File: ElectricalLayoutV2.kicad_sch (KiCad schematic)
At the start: 8 parts, among them J1 PowerBar (24V), J2 PowerBar (Ground), K1 5V-24V (40A), SW1 BFB, SW2 Dead man's switch

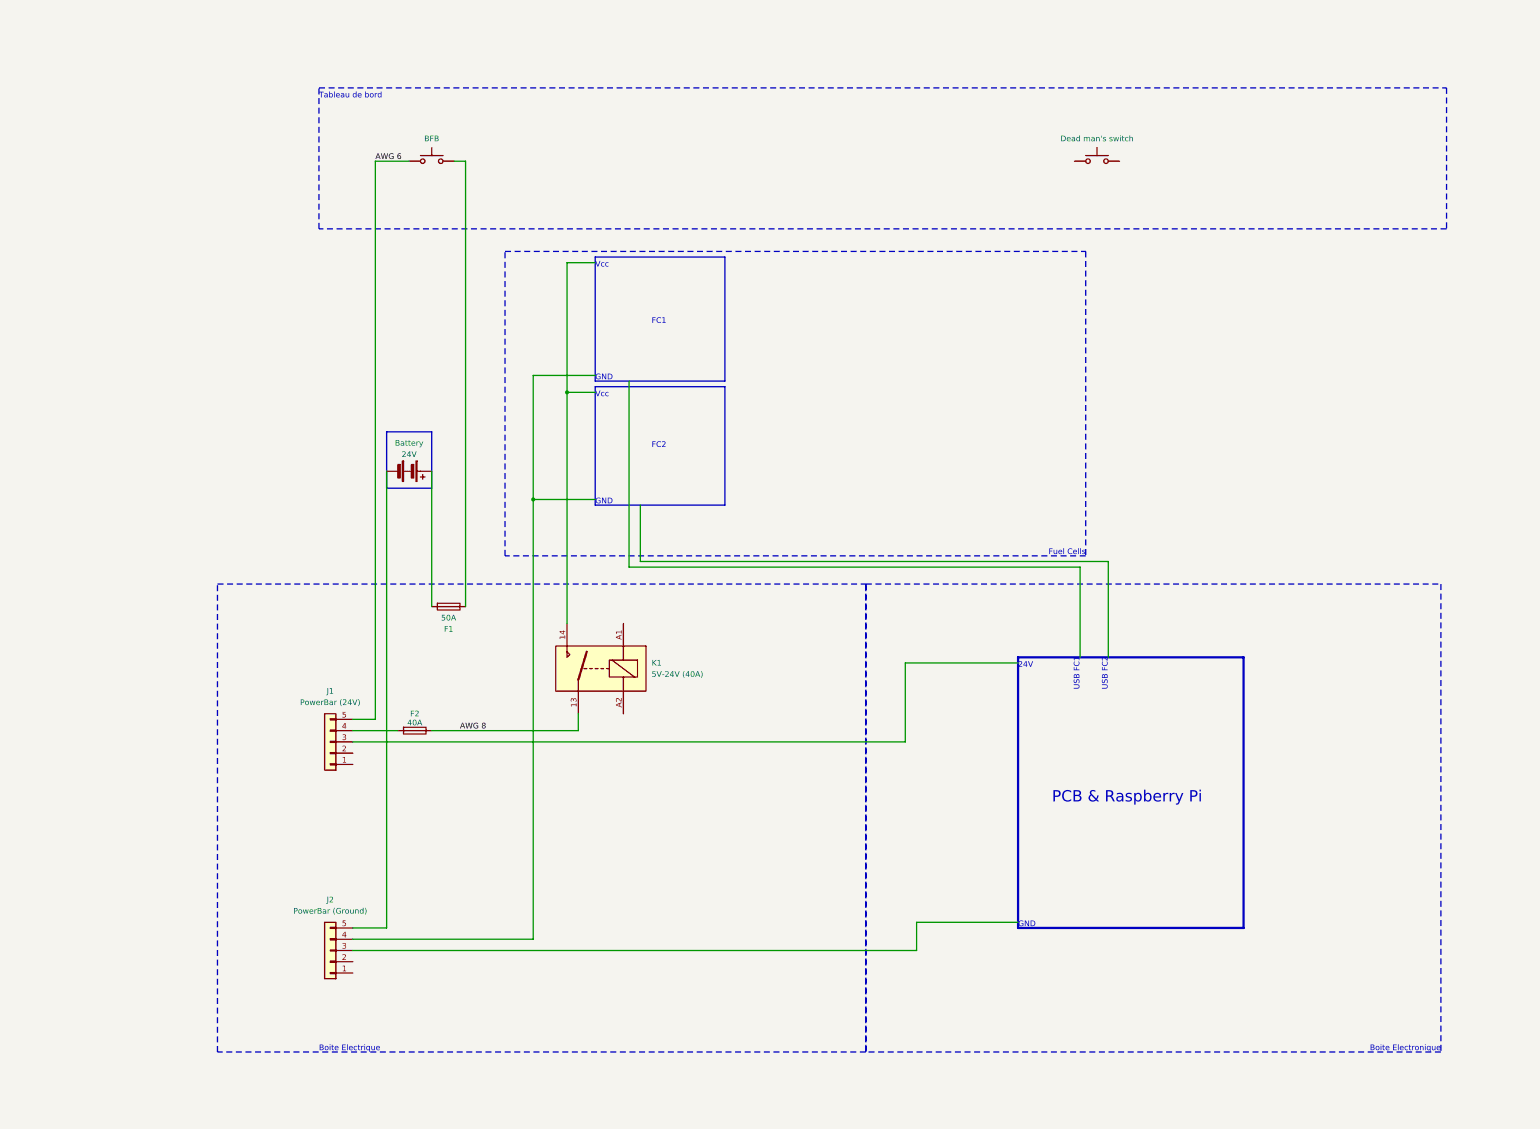
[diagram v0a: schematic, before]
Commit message: Fuel cells and precharge
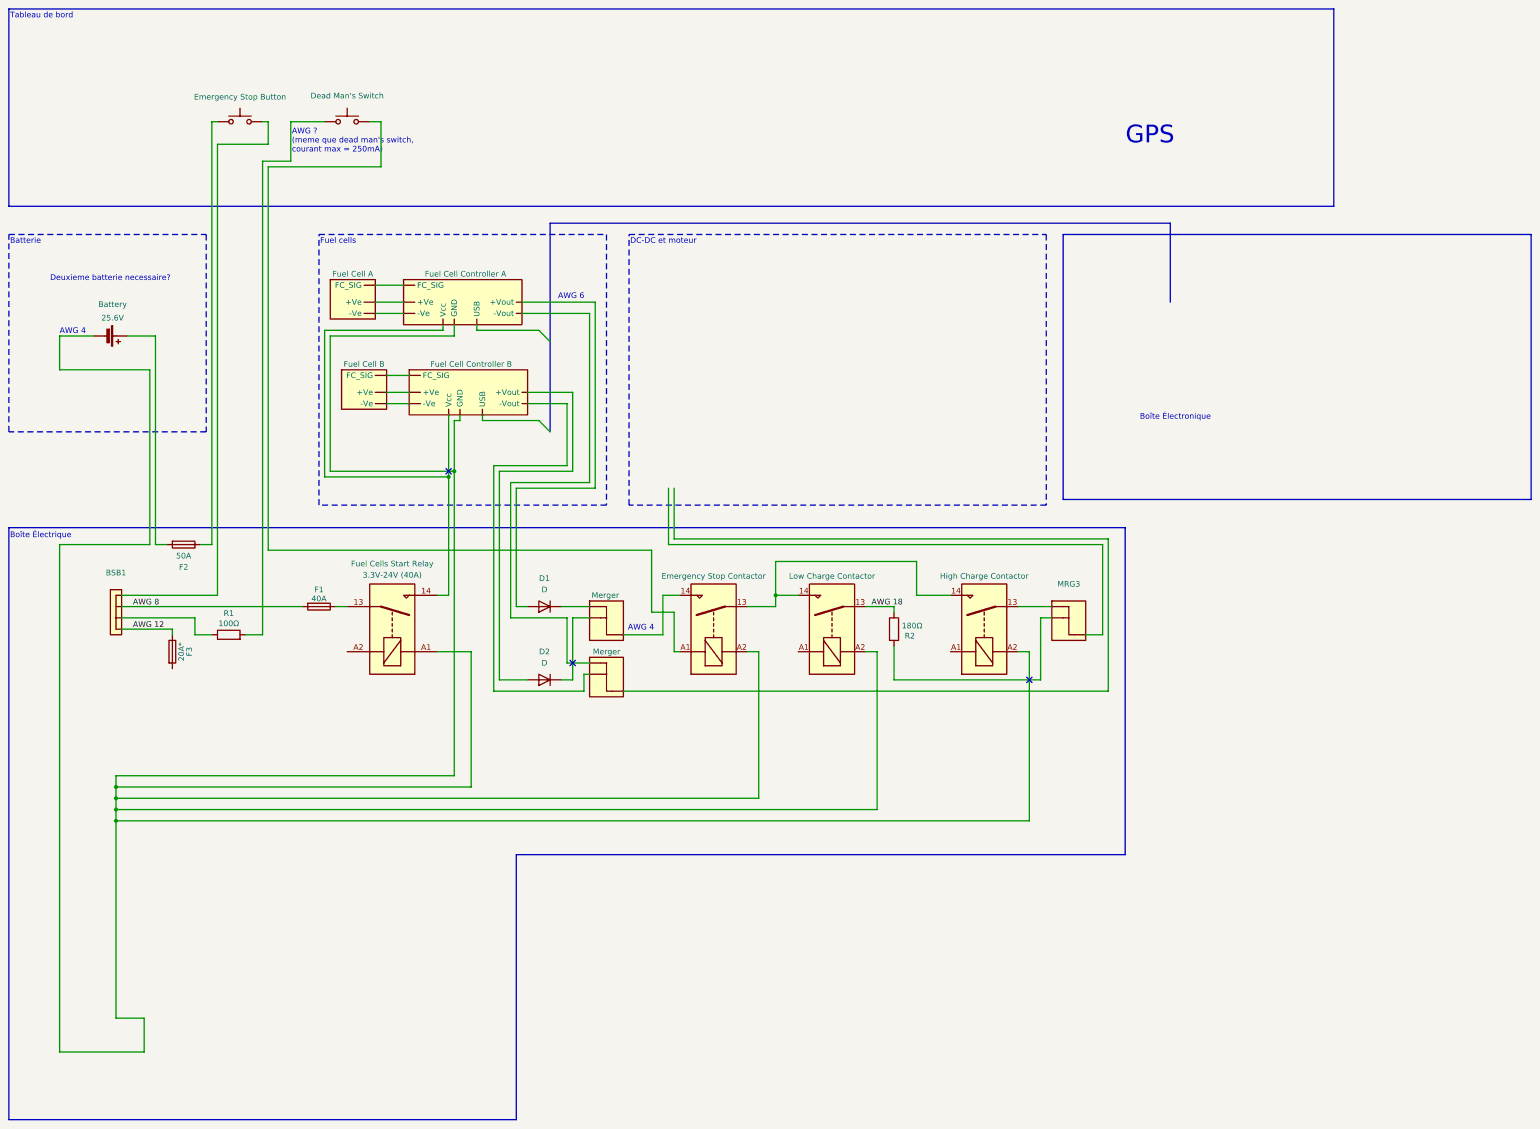
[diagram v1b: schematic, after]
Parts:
- removed BT1: Battery, symbol Device:Battery
- removed J1: PowerBar (24V), symbol Connector_Generic:Conn_01x05
- removed J2: PowerBar (Ground), symbol Connector_Generic:Conn_01x05
- removed SW1: BFB, symbol Switch:SW_MEC_5G
- added B2: 25.6V, symbol Device:Battery_Cell
- added BSB1: ~, symbol Exocet_Electrical:Busbar_4
- added D1, D2: D, symbol Device:D
- added F3: 20A*, symbol Device:Fuse
- added FC3, FC4: ~, symbol Exocet_Electrical:Fuel_Cell
- added FCC1, FCC2: ~, symbol Exocet_Electrical:Fuel_Cell_Controller
- added K2, K3, K4: Relay_SPST-NO, symbol Relay:Relay_SPST-NO
- added MRG1: 50A -> 100A, symbol Exocet_Electrical:Merger_2_1
- added MRG2, MRG3: ~, symbol Exocet_Electrical:Merger_2_1
- added R1: 100Ω, symbol Device:R
- added R2: 180Ω, symbol Device:R
- added SW1: SW_Push, symbol Switch:SW_Push
- K1: value 5V-24V (40A) -> 3.3V-24V (40A); Name (none) -> Fuel Cells Start Relay
- SW2: value Dead man's switch -> ~; Name (none) -> Dead Man's Switch
- renumbered F2 to F1, F1 to F2
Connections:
- net AWG 8: now also F1.2, BSB1.; no longer F1.1, K1.13
- net at F2.1: now also SW1.1
- net at F2.2: now also B2.1 (+)
- net at K1.14: now also FCC1. (Vcc), FCC2. (Vcc)
- net at K1.A1: now also B2.2 (-), FCC1. (Vcc), FCC2. (Vcc), K2.A2, K3.A2, K4.A2
- net at SW2.1: now also R1.2
- net at SW2.2: now also K2.A1
- new net: FC3. (FC_SIG), FCC2. (Vcc) (x3)
- new net: F1.1, K1.13
- new net: BSB1., R1.1
- new net: MRG3., R2.2
- new net: D2.1 (K), MRG1.
- new net: D2.2 (A), FCC1. (Vcc)
- new net: D1.2 (A), FCC2. (Vcc)
- new net: FCC2. (Vcc), MRG2.
- new net: K2.13, K3.14, K4.14
- new net: K2.14, MRG1.
- new net: K4.13, MRG3.
- new net: FC4. (FC_SIG), FCC1. (Vcc) (x3)
- new net: FCC1. (Vcc), MRG2.
- new net: D1.1 (K), MRG1.
- new net: BSB1., SW1.2
- new net AWG 12: BSB1., F3.1
- new net AWG 18: K3.13, R2.1
- no-connect marks 0 -> 3
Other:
- note added: "AWG 4"
- note added: "AWG 6"
- note added: "AWG ? (meme que dead man's switch, courant max = 250mA)"
- note added: "Batterie"
- note added: "Boîte Électrique"
- note added: "Boîte Électronique"
- note added: "DC-DC et moteur"
- note added: "Deuxieme batterie necessaire?"
- note added: "Fuel cells"
- note added: "GPS"
- note removed: "24V"
- note removed: "Boite Electrique"
- note removed: "Boite Electronique"
- note removed: "FC1"
- note removed: "FC2"
- note removed: "Fuel Cells"
- note removed: "GND"
- note removed: "PCB & Raspberry Pi"
- note removed: "USB FC1"
- note removed: "USB FC2"
- note removed: "Vcc"
- moved on the sheet: F1, F2

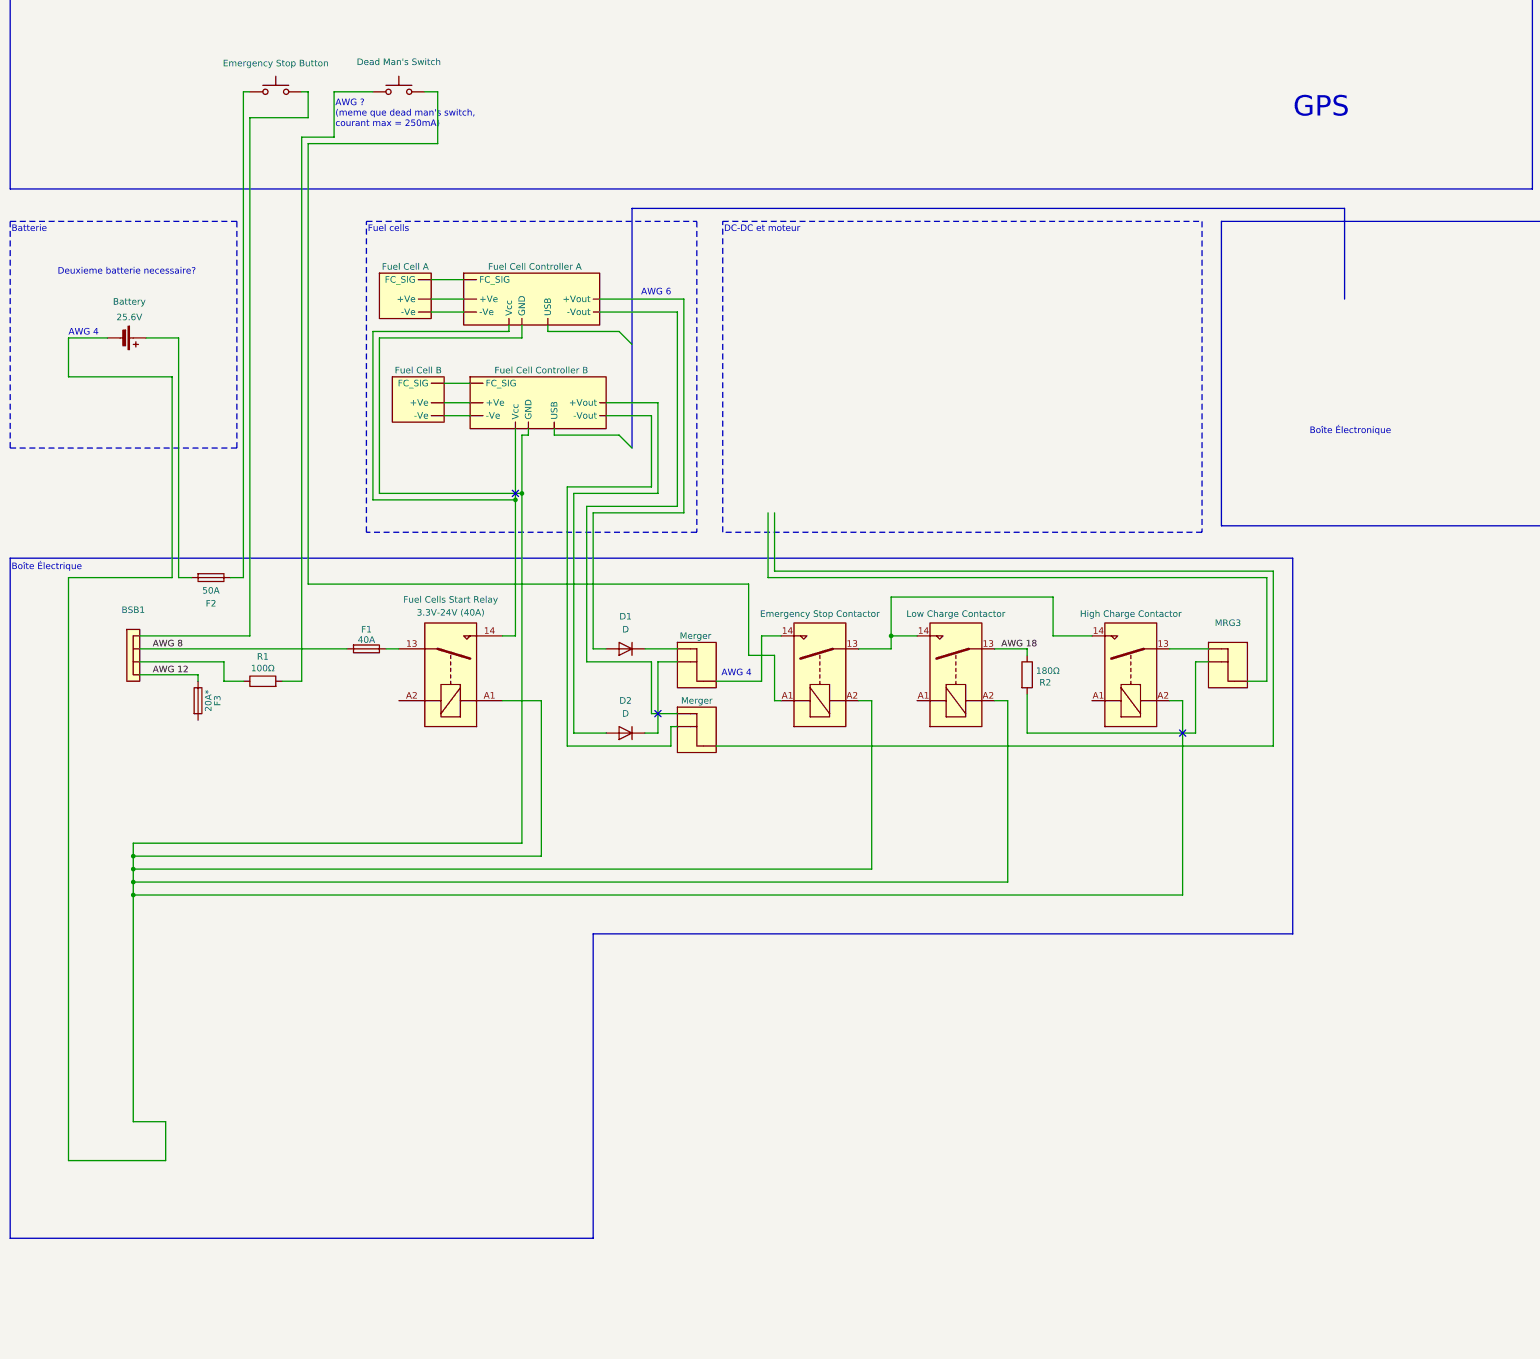
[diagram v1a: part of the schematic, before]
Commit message: Polarity protection and DMS/precharge safety
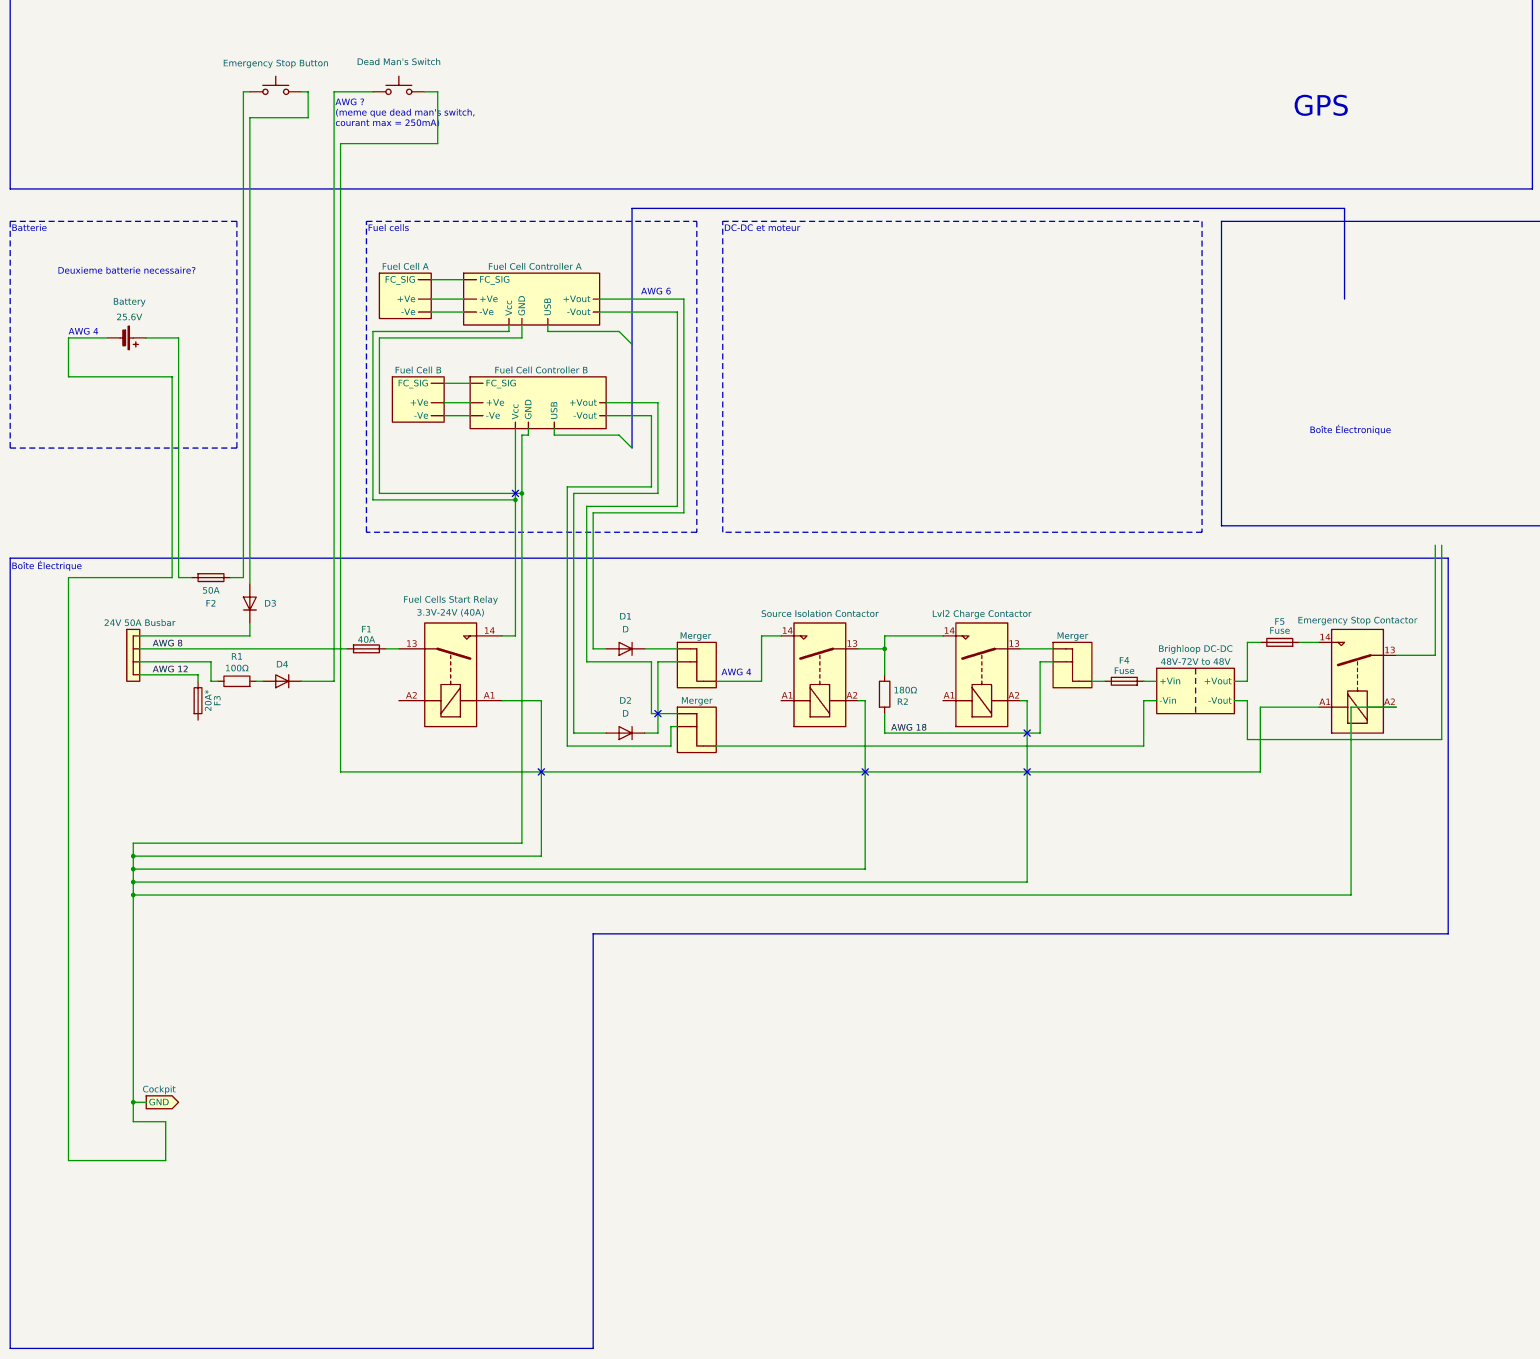
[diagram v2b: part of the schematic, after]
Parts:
- added CGND1: ~, symbol Exocet_Electrical:Cockpit_(grounded)
- added D3, D4: D, symbol Device:D
- added DCC1: 48V-72V to 48V, symbol Exocet_Electrical:Brightloop_DC-DC
- added F4, F5: Fuse, symbol Device:Fuse
- BSB1: Name (none) -> 24V 50A Busbar
- K3: Name Low Charge Contactor -> Source Isolation Contactor
- K4: Name High Charge Contactor -> Lvl2 Charge Contactor
- MRG3: Name (none) -> Merger
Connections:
- net AWG 18: now also MRG3., R2.2; no longer K3.13, R2.1
- net at FCC2. (Vcc): now also MRG2.; no longer FC3. (FC_SIG)
- net at SW2.1: now also D4.1 (K); no longer R1.2
- net at B2.2 (-), FCC1. (Vcc), FCC2. (Vcc)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: now also CGND1. (GND)
- net at MRG2.: now also FCC1. (Vcc); no longer FCC2. (Vcc)
- net at K2.14: now also F5.2; no longer MRG1.
- net at SW1.2: now also D3.2 (A); no longer BSB1.
- new net: FC3. (FC_SIG), FCC2. (Vcc) (x2)
- new net: D4.2 (A), R1.2
- new net: DCC1. (-Vout), F4.2
- new net: DCC1. (-Vout), F5.1
- new net: DCC1. (-Vout), MRG2.
- new net: K3.13, K4.14, R2.1
- new net: F4.1, MRG3.
- new net: K3.14, MRG1.
- new net: FCC1. (Vcc), FCC2. (Vcc), K1.14
- new net: FC4. (FC_SIG), FCC1. (Vcc) (x2)
- new net: BSB1., D3.1 (K)
- now unconnected: K2.13
- no-connect marks 3 -> 6
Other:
- moved on the sheet: R1, R2

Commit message: Motor and sheet layout improvement
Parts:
- added D5: D, symbol Device:D
- added F6: Fuse, symbol Device:Fuse
- added PROP1: 5kW / 48V, symbol Exocet_Electrical:Outboard_5.0
- added R3: 180Ω, symbol Device:R
- added SW3: SW_Push, symbol Switch:SW_Push
- added THR1: ~, symbol Exocet_Electrical:Throttle
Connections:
- net AWG 12: now also F3.2; no longer F3.1
- net AWG 18: now also K3.13, K4.14, R2.1; no longer MRG3., R2.2
- net at K2.13: now also F6.2
- net at K2.A1: now also D4.1 (K); no longer SW2.2
- net at FCC2. (Vcc): now also MRG2.; no longer FC3. (FC_SIG)
- net at SW2.1: now also R1.1; no longer D4.1 (K)
- net at R1.2: now also BSB1.; no longer D4.2 (A)
- net at DCC1. (-Vout): now also F5.1
- net at MRG2.: now also FCC1. (Vcc); no longer DCC1. (-Vout)
- net at F4.1, MRG3.: now also R3.2
- new net: FC3. (FC_SIG), FCC2. (Vcc) (x2)
- new net: DCC1. (-Vout), PROP1. (Vcc)
- new net: DCC1. (-Vout), MRG2., SW3.2
- new net: D5.1 (K), PROP1. (Vcc)
- new net: D5.2 (A), F6.1
- new net: R3.1, SW3.1
- new net: FCC1. (Vcc), FCC2. (Vcc), K1.14
- new net: FC4. (FC_SIG), FCC1. (Vcc) (x2)
- new net: MRG3., R2.2
- new net: D4.2 (A), SW2.2
- no-connect marks 6 -> 3
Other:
- note added: "Battery"
- note added: "Dashboard"
- note added: "Electronics Box"
- note added: "H2 Plate"
- note added: "High Power Box"
- note added: "Motor & Throttle"
- note added: "NOTES"
- note removed: "Batterie"
- note removed: "Boîte Électrique"
- note removed: "Boîte Électronique"
- note removed: "DC-DC et moteur"
- note removed: "Deuxieme batterie necessaire?"
- note removed: "GPS"
- note removed: "Tableau de bord"
- company: (none) -> Exocet Polytechnique Montréal
- title: (none) -> Electrical Layout 2024
- moved on the sheet: D1, D2, D3, F1, F4, F5
